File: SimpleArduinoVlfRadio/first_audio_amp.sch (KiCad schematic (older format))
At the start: 10 parts, among them Q2 PN2222A

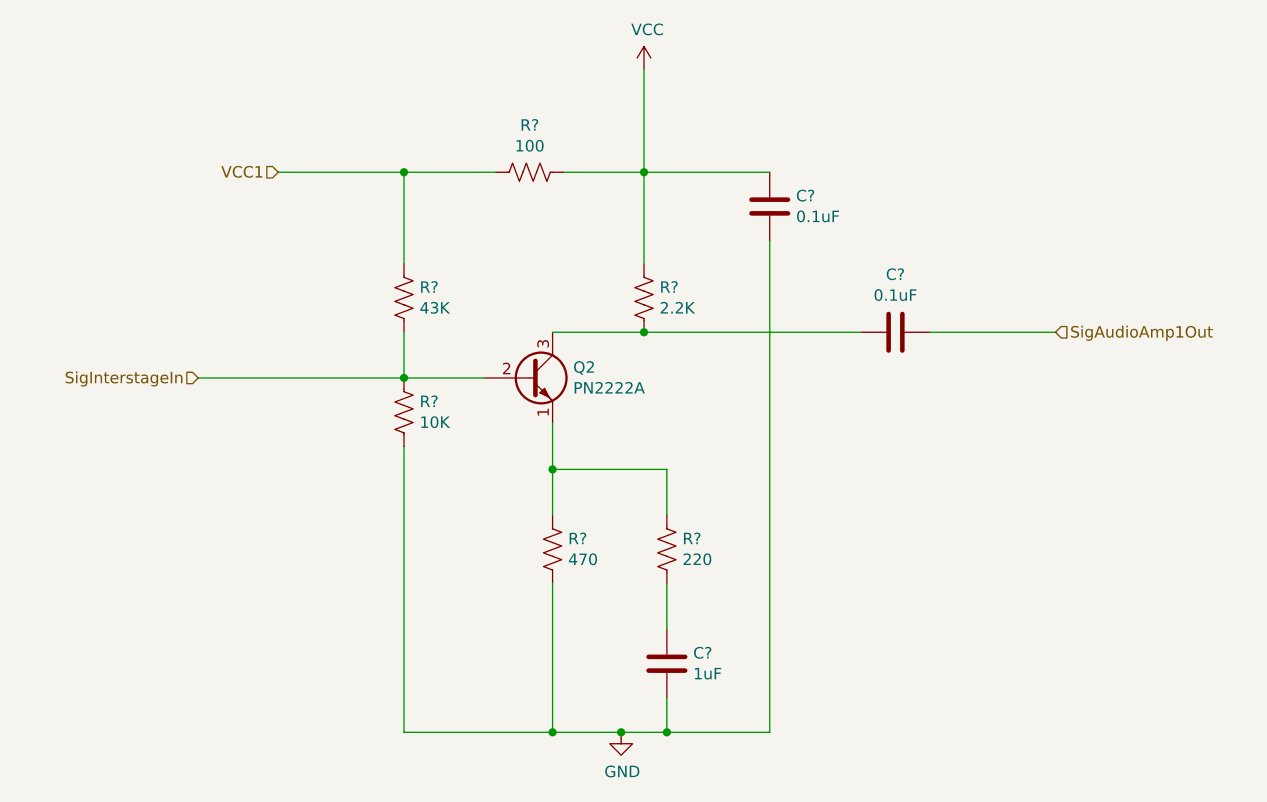
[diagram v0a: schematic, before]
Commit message: R value fix
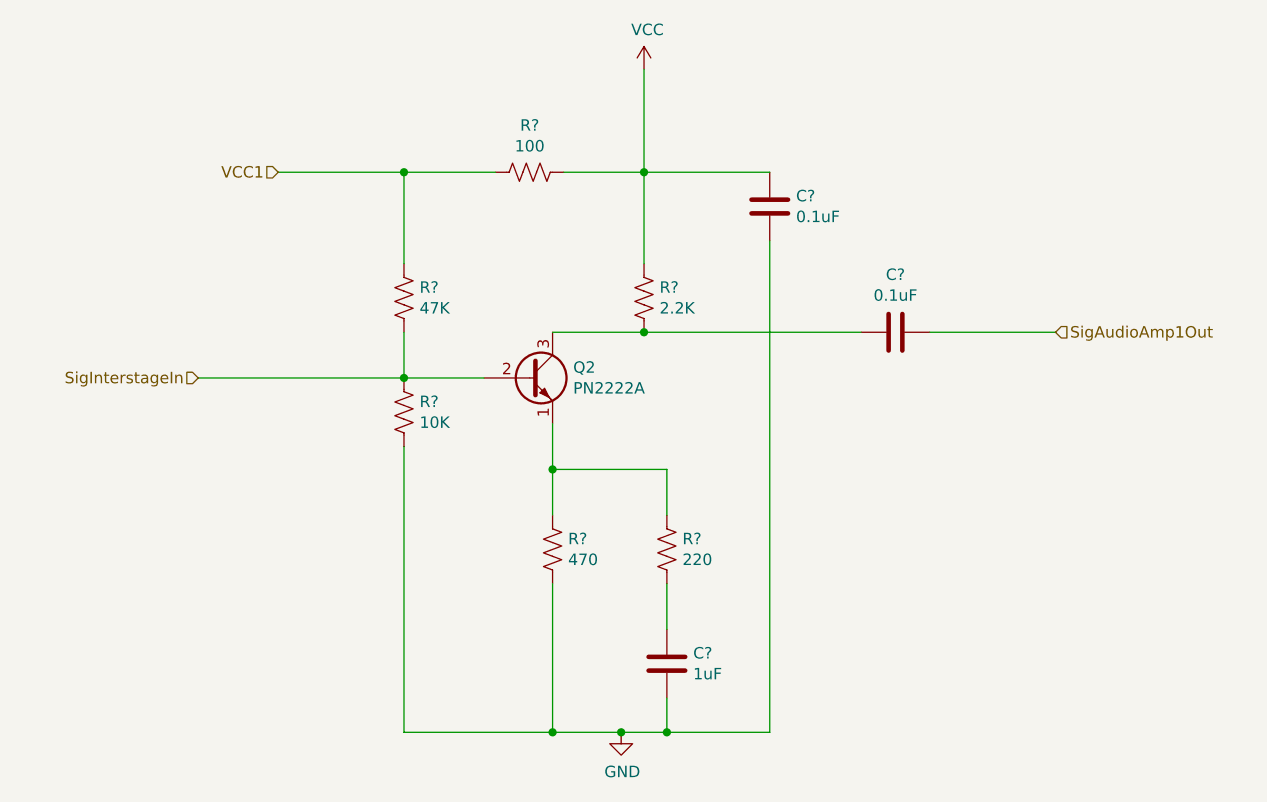
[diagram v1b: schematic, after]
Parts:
- R?: value 43K -> 47K
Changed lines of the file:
@@
 P 5000 3400
 F 0 "R?" H 5068 3446 50  0000 L CNN
-F 1 "43K" H 5068 3355 50  0000 L CNN
+F 1 "47K" H 5068 3355 50  0000 L CNN
 F 2 "" V 5040 3390 50  0001 C CNN
 F 3 "~" H 5000 3400 50  0001 C CNN
